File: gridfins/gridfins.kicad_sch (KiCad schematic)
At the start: 45 parts, among them J1 RBUS, U1 ESP32-S3, Y1 R940000171

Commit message: update 3
added tvs diode chip module for 3rd servo
added net connection to actuators sheet
changed 6 to 7.4 label
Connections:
- net SERVOPWM0: now reaches U1.39 (GPIO34)
- net SERVOPWM1: now reaches U1.40 (GPIO35)
- net SERVOPWM2: now reaches U1.41 (GPIO36)
- net +6V renamed +7.4V
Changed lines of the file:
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@@
 	(wire
 		(pts
+			(xy 208.28 137.16) (xy 222.25 137.16)
+		)
+		(stroke
+			(width 0)
+			(type default)
+		)
+	)
+	(wire
+		(pts
 			(xy 57.15 147.32) (xy 59.69 147.32)
 		)
@@
 	(wire
 		(pts
+			(xy 208.28 129.54) (xy 222.25 129.54)
+		)
+		(stroke
+			(width 0)
+			(type default)
+		)
+	)
+	(wire
+		(pts
 			(xy 59.69 67.31) (xy 69.85 67.31)
 		)
@@
 	(wire
 		(pts
+			(xy 208.28 133.35) (xy 222.25 133.35)
+		)
+		(stroke
+			(width 0)
+			(type default)
+		)
+	)
+	(wire
+		(pts
 			(xy 30.48 191.77) (xy 39.37 191.77)
 		)
@@
 		)
 	)
+	(label "SERVOPWM0"
+		(at 135.89 97.79 0)
+		(effects
+			(font
+				(size 1.27 1.27)
+			)
+			(justify left bottom)
+		)
+	)
+	(label "SERVOPWM0"
+		(at 208.28 129.54 0)
+		(effects
+			(font
+				(size 1.27 1.27)
+			)
+			(justify left bottom)
+		)
+	)
 	(label "CHIP_PU"
 		(at 36.83 165.1 180)
@@
 		)
 	)
+	(label "SERVOPWM1"
+		(at 208.28 133.35 0)
+		(effects
+			(font
+				(size 1.27 1.27)
+			)
+			(justify left bottom)
+		)
+	)
+	(label "SERVOPWM1"
+		(at 135.89 100.33 0)
+		(effects
+			(font
+				(size 1.27 1.27)
+			)
+			(justify left bottom)
+		)
+	)
 	(label "BuckPGOOD"
 		(at 262.89 106.68 0)
@@
 		)
 	)
+	(label "SERVOPWM2"
+		(at 135.89 102.87 0)
+		(effects
+			(font
+				(size 1.27 1.27)
+			)
+			(justify left bottom)
+		)
+	)
 	(label "BOOT"
 		(at 68.58 165.1 180)
@@
 		)
 	)
+	(label "SERVOPWM2"
+		(at 208.28 137.16 0)
+		(effects
+			(font
+				(size 1.27 1.27)
+			)
+			(justify left bottom)
+		)
+	)
 	(label "CHIP_PU"
 		(at 39.37 191.77 180)
@@
 			)
 		)
-		(property "Value" "+6V"
-			(at 205.2153 87.0278 0)
+		(property "Value" "+7.4V"
+			(at 204.724 86.868 0)
 			(effects
 				(font

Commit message: Update with Inertial Measurement Unit
cloned IMU from pickle rick.
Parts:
- added TP25, TP26, TP27: TestPoint, TestPoint:TestPoint_Pad_D1.0mm, symbol Connector:TestPoint
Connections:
- net HSPI_MISO: now reaches U1.13 (GPIO8/ADC1_CH7)
- net HSPI_MOSI: now reaches U1.14 (GPIO9/ADC1_CH8)
- net HSPI_SCLK: now reaches U1.15 (GPIO10/ADC1_CH9)
- net IMU1_CS: now reaches U1.16 (GPIO11/ADC2_CH0)
- net IMU1_CS: now also TP26.1
- net IMU2_CS: now reaches U1.17 (GPIO12/ADC2_CH1)
- net IMU2_CS: now also TP25.1
- net MAG_CS: now reaches U1.18 (GPIO13/ADC2_CH2)
- net MAG_CS: now also TP27.1
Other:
- added sheet IMU (IMU.kicad_sch)
- moved on the sheet: D3, R19

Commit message: forgot to save the file
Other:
- sheet Servo-Actuators renamed Servo
- added sheet Linear Actuator (LinearActuator.kicad_sch)
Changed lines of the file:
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@@
 	(wire
 		(pts
-			(xy 208.28 137.16) (xy 222.25 137.16)
+			(xy 208.28 124.46) (xy 222.25 124.46)
 		)
 		(stroke
@@
 	(wire
 		(pts
-			(xy 208.28 129.54) (xy 222.25 129.54)
+			(xy 208.28 116.84) (xy 222.25 116.84)
 		)
 		(stroke
@@
 	(wire
 		(pts
-			(xy 208.28 133.35) (xy 222.25 133.35)
+			(xy 208.28 120.65) (xy 222.25 120.65)
 		)
 		(stroke
@@
 	)
 	(label "SERVOPWM0"
-		(at 208.28 129.54 0)
+		(at 208.28 116.84 0)
 		(effects
 			(font
@@
 	)
 	(label "SERVOPWM1"
-		(at 208.28 133.35 0)
+		(at 208.28 120.65 0)
 		(effects
 			(font
@@
 	)
 	(label "SERVOPWM2"
-		(at 208.28 137.16 0)
+		(at 208.28 124.46 0)
 		(effects
 			(font
@@
 	)
 	(sheet
-		(at 222.25 123.19)
-		(size 38.1 21.59)
+		(at 222.25 113.03)
+		(size 15.24 15.24)
 		(exclude_from_sim no)
 		(in_bom yes)
@@
 			(color 0 0 0 0.0000)
 		)
-		(property "Sheetname" "Servo-Actuators"
-			(at 222.25 122.4784 0)
+		(property "Sheetname" "Servo"
+			(at 222.25 112.3184 0)
 			(effects
 				(font
@@
 		)
 		(property "Sheetfile" "actuators.kicad_sch"
-			(at 222.25 145.3646 0)
+			(at 222.25 128.8546 0)
 			(effects
 				(font
@@
 		)
 		(pin "Servo_0_PWM" input
-			(at 222.25 129.54 180)
+			(at 222.25 116.84 180)
 			(effects
 				(font
@@
 		)
 		(pin "Servo_1_PWM" input
-			(at 222.25 133.35 180)
+			(at 222.25 120.65 180)
 			(effects
 				(font
@@
 		)
 		(pin "Servo_2_PWM" input
-			(at 222.25 137.16 180)
+			(at 222.25 124.46 180)
 			(effects
 				(font
@@
 				)
 			)
+		)
+	)
+	(sheet
+		(at 222.25 139.7)
+		(size 15.24 10.16)
+		(exclude_from_sim no)
+		(in_bom yes)
+		(on_board yes)
+		(dnp no)
+		(fields_autoplaced yes)
+		(stroke
+			(width 0.1524)
+			(type solid)
+		)
+		(fill
+			(color 0 0 0 0.0000)
+		)
+		(property "Sheetname" "Linear Actuator"
+			(at 222.25 138.9884 0)
+			(effects
+				(font
+					(size 1.27 1.27)
+				)
+				(justify left bottom)
+			)
+		)
+		(property "Sheetfile" "LinearActuator.kicad_sch"
+			(at 222.25 150.4446 0)
+			(effects
+				(font
+					(size 1.27 1.27)
+				)
+				(justify left top)
+			)
+		)
+		(instances
+			(project "gridfins"
+				(path "/7db990e4-92e1-4f99-b4d2-435bbec1ba83"
+					(page "8")
+				)
+			)

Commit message: SD card, linear actuator encoders
Imported microSD reader from Stark

Added pin connectors and SPI routes for AS5048 magnetic rotary encoder to be used with the linear actuator/brushed motor

Added test pads for SD reader and encoder chip select
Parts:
- added TP3, TP7: TestPoint, TestPoint:TestPoint_Pad_D1.0mm, symbol Connector:TestPoint
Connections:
- net HSPI_MISO: now also U1.14 (GPIO9/ADC1_CH8); no longer U1.13 (GPIO8/ADC1_CH7)
- net HSPI_MOSI: now also U1.15 (GPIO10/ADC1_CH9); no longer U1.14 (GPIO9/ADC1_CH8)
- net HSPI_SCLK: now also U1.16 (GPIO11/ADC2_CH0); no longer U1.15 (GPIO10/ADC1_CH9)
- net IMU1_CS: now also U1.17 (GPIO12/ADC2_CH1); no longer U1.16 (GPIO11/ADC2_CH0)
- net IMU2_CS: now also U1.18 (GPIO13/ADC2_CH2); no longer U1.17 (GPIO12/ADC2_CH1)
- net MAG_CS: now also U1.19 (GPIO14/ADC2_CH3); no longer U1.18 (GPIO13/ADC2_CH2)
- net SD1_CS: now reaches U1.10 (GPIO5/ADC1_CH4)
- net SD1_CS: now also TP7.1
- net VSPI_MOSI: now reaches U1.11 (GPIO6/ADC1_CH5)
- net VSPI_SCLK: now reaches U1.12 (GPIO7/ADC1_CH6)
- net ENCODER_CS: now reaches U1.43 (GPIO38)
- net ENCODER_CS: now also TP3.1
- net BUCK_EN: now reaches U1.51 (GPIO45)
- net SD1_DET: now reaches U1.7 (GPIO2/ADC1_CH1)
- net SD_EN: now reaches U1.9 (GPIO4/ADC1_CH3)
- new net VSPI_MISO: U1.13 (GPIO8/ADC1_CH7)
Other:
- added sheet microSD reader (SD_sch.kicad_sch)
- sheet Linear Actuator ports: added ENCODER_CS, VSPI_CLK, VSPI_MISO, VSPI_MOSI; removed none
- moved on the sheet: R34

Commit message: Deployment Power Cut Mechanism
Employed the master high-side switch from flintandsteel to disable servo and linear actuator power once lower altitude limit reached. This will prevent electrical problems during touchdown:

Routed power rail 16.8V to switch input. Switch output routed to buck input. When high-side switch is enabled, buck input voltage is pulled down, depowering the servos and linear actuator.
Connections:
- net HSIDE_EN: now reaches U1.42 (GPIO37)
- net BUS_VMON: now reaches U1.6 (GPIO1/ADC1_CH0)
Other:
- added sheet master high side switch (highside.kicad_sch)
- sheet Buck ports: added VINBuck; removed none

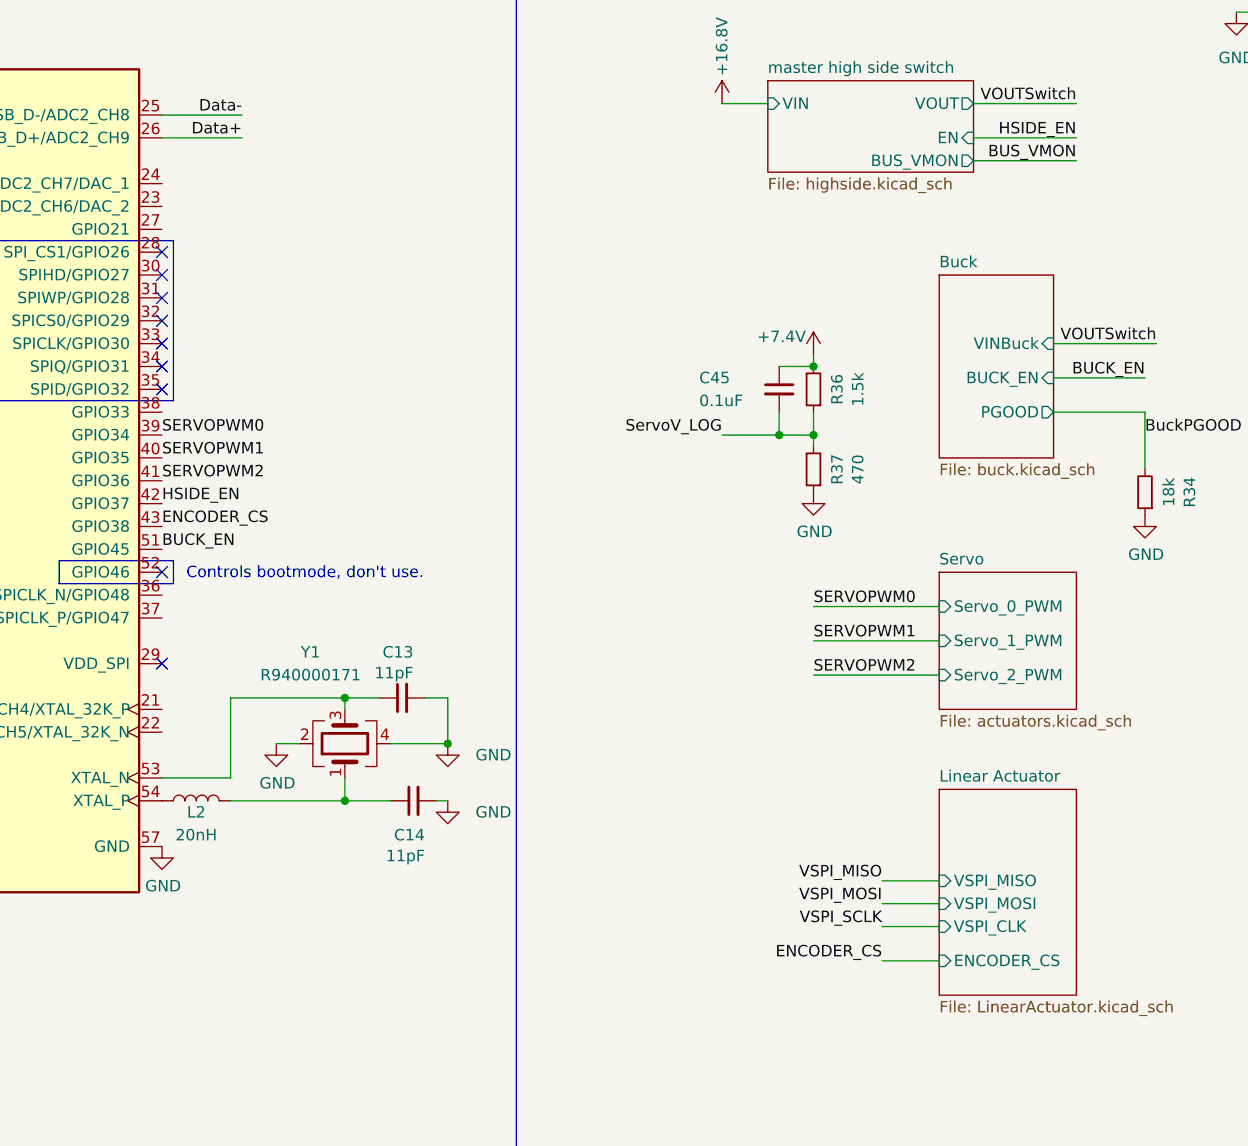
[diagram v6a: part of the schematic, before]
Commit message: First Attempt connection of stepper motor driver for linear actuator
Added connections of driver and 4 pin nano. Added hierarchical labels and connected to GPIO. Current configuration is the INDEX mode
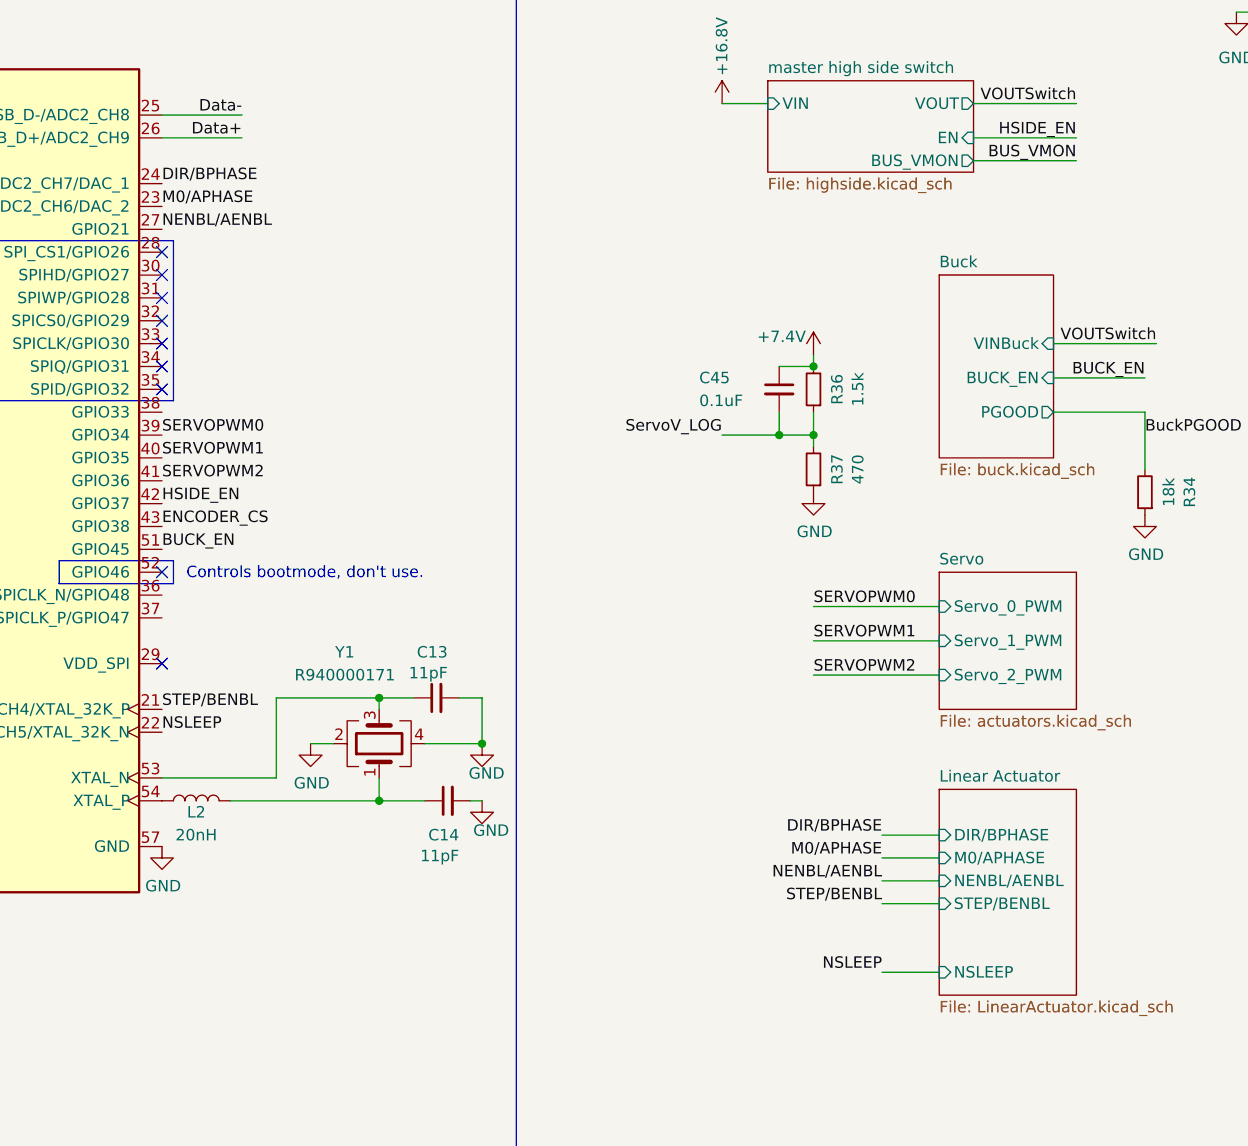
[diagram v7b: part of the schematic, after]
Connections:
- net STEP/BENBL: now reaches U1.21 (GPIO15/ADC2_CH4/XTAL_32K_P)
- net NSLEEP: now reaches U1.22 (GPIO16/ADC2_CH5/XTAL_32K_N)
- net M0/APHASE: now reaches U1.23 (GPIO17/ADC2_CH6/DAC_2)
- net DIR/BPHASE: now reaches U1.24 (GPIO18/ADC2_CH7/DAC_1)
- net NENBL/AENBL: now reaches U1.27 (GPIO21)
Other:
- sheet Linear Actuator ports: added DIR/BPHASE, M0/APHASE, NENBL/AENBL, NSLEEP, STEP/BENBL; removed ENCODER_CS, VSPI_CLK, VSPI_MISO, VSPI_MOSI
- moved on the sheet: C13, C14, Y1

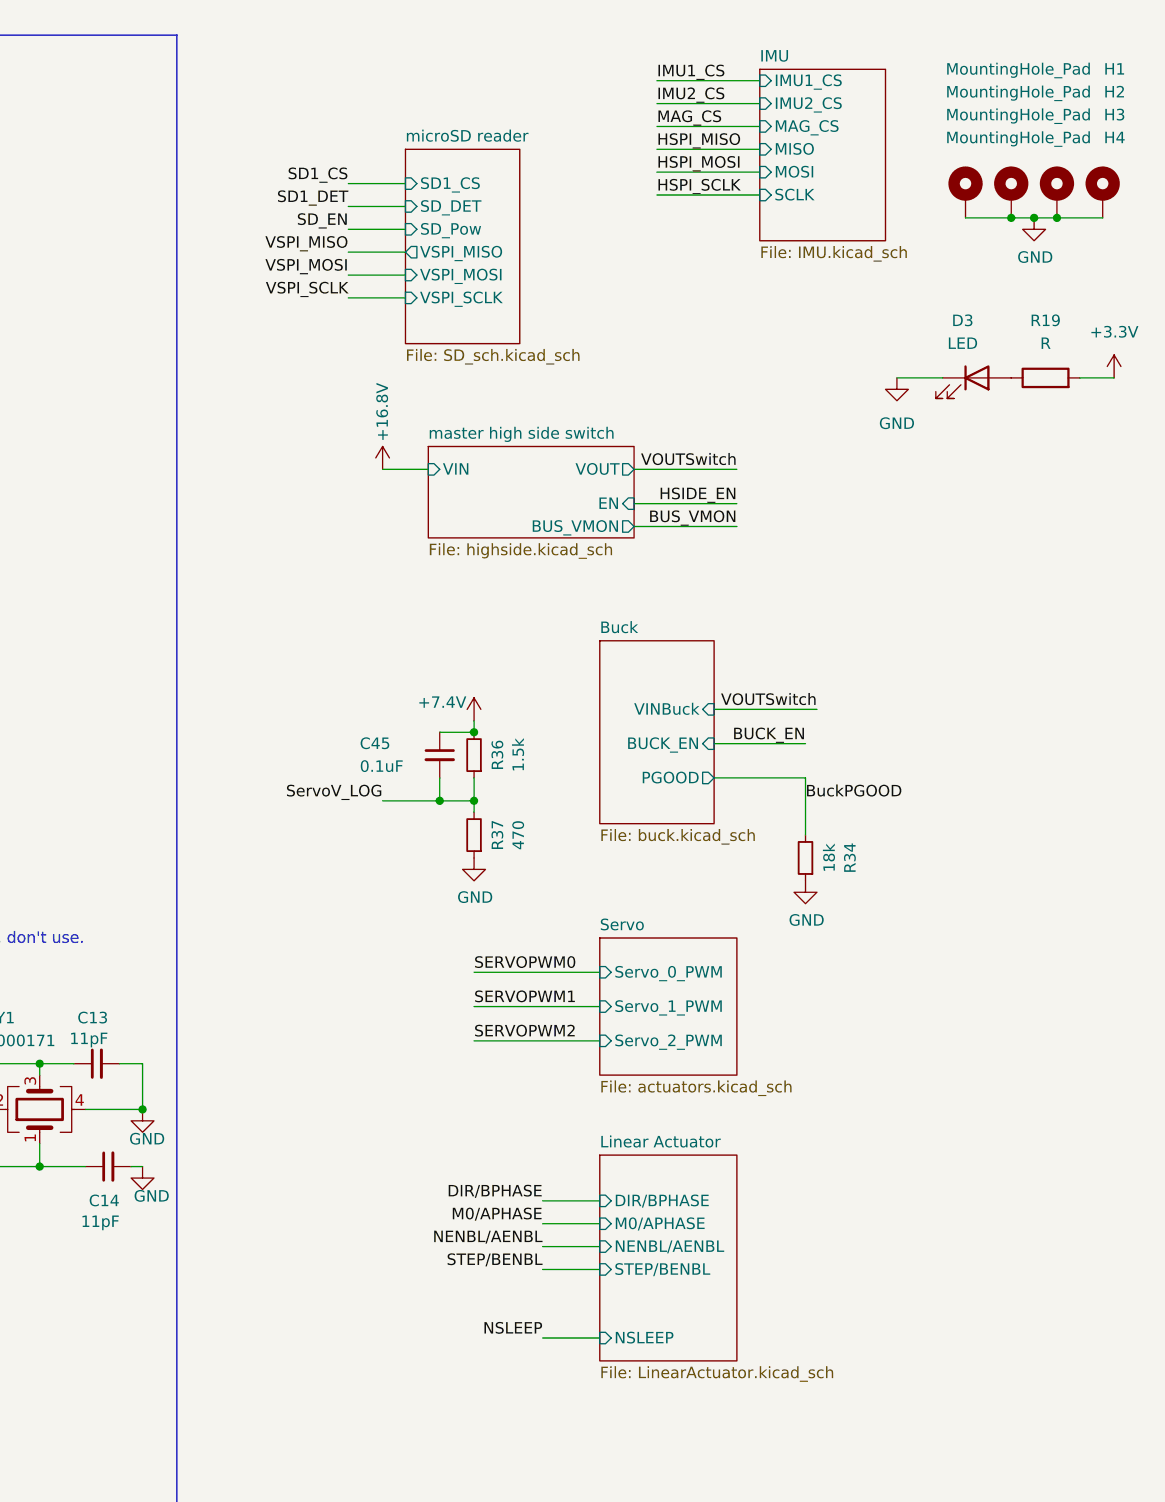
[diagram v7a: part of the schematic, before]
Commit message: Power distribution rework
Added missing main power supply voltage to Stepper Motor Driver Board

Separate Buck converter for servo and linear actuator(stepper motor)

16.8V -> Buck -> high side switch -> H-bridge -> 10V
16.8V -> Buck -> Servo -> 7.4V
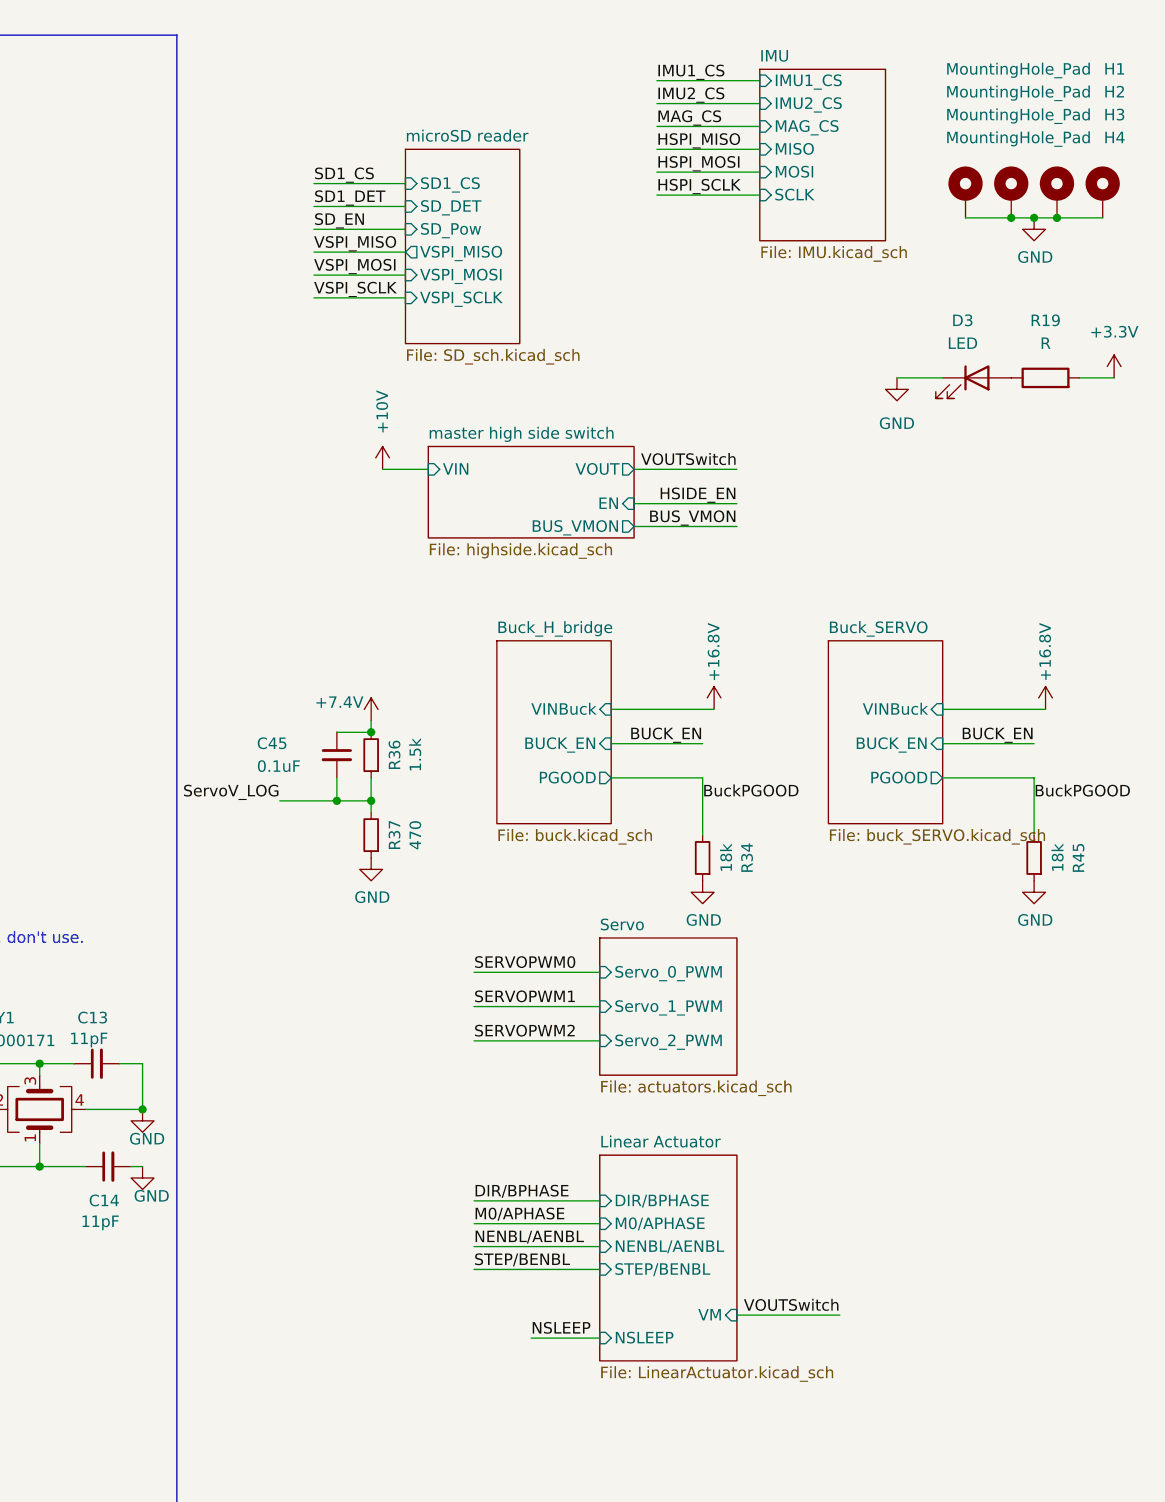
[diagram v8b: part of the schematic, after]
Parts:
- added R45: 18k, Resistor_SMD:R_0402_1005Metric, symbol Device:R_Small
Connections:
- net BuckPGOOD: now also R45.2
- net GND: now also R45.1
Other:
- sheet Buck renamed Buck_H_bridge
- added sheet Buck_SERVO (buck_SERVO.kicad_sch)
- sheet Linear Actuator ports: added VM; removed none
- moved on the sheet: C45, R34, R36, R37
